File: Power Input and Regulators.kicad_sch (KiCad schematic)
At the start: 26 parts, among them J403 Screw_Terminal_01x03, U11 LD1117S33TR_SOT223, U12 LD1117S18TR_SOT223

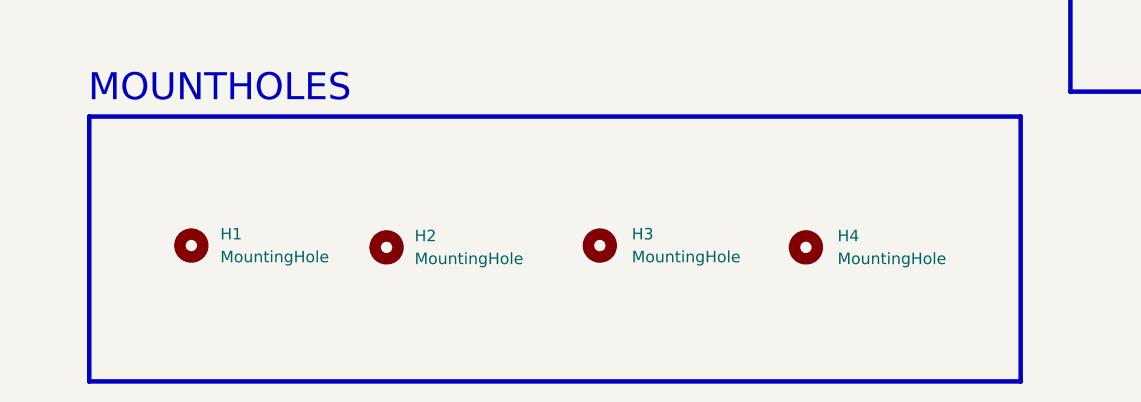
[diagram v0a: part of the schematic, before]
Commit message: All tracks routed, ERC done, waiting for PDN Analysis.
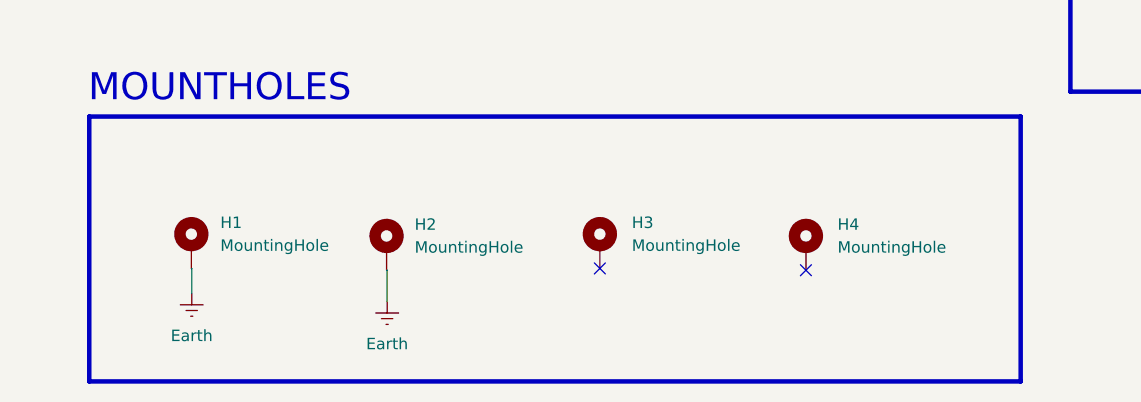
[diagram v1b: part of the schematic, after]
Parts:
- H1, H2, H3, H4: footprint MountingHole:MountingHole_2.1mm -> MountingHole:MountingHole_2.2mm_M2_DIN965_Pad; symbol Mechanical:MountingHole -> Mechanical:MountingHole_Pad; now left out of the parts list
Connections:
- new net Earth: H1.1, H2.1
- no-connect marks 0 -> 2
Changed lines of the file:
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@@
 		(color 0 0 0 0)
 	)
+	(no_connect
+		(at 122.221 152.7349)
+	)
+	(no_connect
+		(at 99.3247 152.5341)
+	)
 	(wire
 		(pts
@@
 	(wire
 		(pts
+			(xy 75.6884 156.2136) (xy 75.6884 152.7349)
+		)
+		(stroke
+			(width 0)
+			(type default)
+		)
+	)
+	(wire
+		(pts
 			(xy 183.6373 111.1069) (xy 183.6373 107.1757)
 		)
@@
 	(wire
 		(pts
+			(xy 53.9747 152.5341) (xy 53.934 152.5341)
+		)
+		(stroke
+			(width 0)
+			(type default)
+		)
+	)
+	(wire
+		(pts
 			(xy 58.4554 69.5105) (xy 58.4554 69.5604)
 		)
@@
 	(wire
 		(pts
+			(xy 75.6884 152.7349) (xy 75.6251 152.7349)
+		)
+		(stroke
+			(width 0)
+			(type default)
+		)
+	)
+	(wire
+		(pts
 			(xy 191.2089 122.2781) (xy 191.2089 122.441)
 		)
@@
 	(wire
 		(pts
+			(xy 53.9747 155.3066) (xy 53.9747 152.5341)
+		)
+		(stroke
+			(width 0)
+			(type default)
+		)
+	)
+	(wire
+		(pts
 			(xy 154.1008 47.327) (xy 154.1008 52.0459)
 		)
@@
 	)
 	(symbol
-		(lib_id "Mechanical:MountingHole")
+		(lib_id "Mechanical:MountingHole_Pad")
 		(at 99.3247 149.9941 0)
 		(unit 1)
-		(exclude_from_sim no)
-		(in_bom yes)
+		(exclude_from_sim yes)
+		(in_bom no)
 		(on_board yes)
 		(dnp no)
 		(fields_autoplaced yes)
 		(property "Reference" "H3"
-			(at 102.87 148.724 0)
+			(at 102.87 147.454 0)
 			(effects
 				(font
@@
 		)
 		(property "Value" "MountingHole"
-			(at 102.87 151.264 0)
+			(at 102.87 149.994 0)
 			(effects
 				(font
@@
 			)
 		)
-		(property "Footprint" "MountingHole:MountingHole_2.1mm"
+		(property "Footprint" "MountingHole:MountingHole_2.2mm_M2_DIN965_Pad"
 			(at 99.3247 149.9941 0)
 			(effects
@@
 			)
 		)
-		(property "Description" "Mounting Hole without connection"
+		(property "Description" "Mounting Hole with connection"
 			(at 99.3247 149.9941 0)
 			(effects
@@
 			)
 		)
+		(pin "1"
+		)
 		(instances
 			(project ""
@@
 	)
 	(symbol
+		(lib_id "power:Earth")
+		(at 53.9747 155.3066 0)
+		(unit 1)
+		(exclude_from_sim no)
+		(in_bom yes)
+		(on_board yes)
+		(dnp no)
+		(fields_autoplaced yes)
+		(property "Reference" "#PWR0416"
+			(at 53.9747 161.6566 0)
+			(effects
+				(font
+					(size 1.27 1.27)
+				)
+				(hide yes)
+			)
+		)
+		(property "Value" "Earth"
+			(at 53.9747 160.02 0)
+			(effects
+				(font
+					(size 1.27 1.27)
+				)
+			)
+		)
+		(property "Footprint" ""
+			(at 53.9747 155.3066 0)
+			(effects
+				(font
+					(size 1.27 1.27)
+				)
+				(hide yes)
+			)
+		)
+		(property "Datasheet" "~"
+			(at 53.9747 155.3066 0)
+			(effects
+				(font
+					(size 1.27 1.27)
+				)
+				(hide yes)
+			)
+		)
+		(property "Description" "Power symbol creates a global label with name \"Earth\""
+			(at 53.9747 155.3066 0)
+			(effects
+				(font
+					(size 1.27 1.27)
+				)
+				(hide yes)
+			)
+		)
+		(pin "1"
+		)
+		(instances
+			(project ""
+				(path "/8a424437-6f3e-424c-a786-3b8b285eee60/89ed5f6c-6a59-4754-9fdb-29c83f804302"
+					(reference "#PWR0416")
+					(unit 1)
+				)
+			)
+		)
+	)
+	(symbol
 		(lib_id "power:+12V")
 		(at 155.0312 102.4533 0)
@@
 	)
 	(symbol
+		(lib_id "power:Earth")
+		(at 75.6884 156.2136 0)
+		(unit 1)
+		(exclude_from_sim no)
+		(in_bom yes)
+		(on_board yes)
+		(dnp no)
+		(fields_autoplaced yes)
+		(property "Reference" "#PWR0102"
+			(at 75.6884 162.5636 0)
+			(effects
+				(font
+					(size 1.27 1.27)
+				)
+				(hide yes)
+			)
+		)
+		(property "Value" "Earth"
+			(at 75.6884 160.927 0)
+			(effects
+				(font
+					(size 1.27 1.27)
+				)
+			)
+		)
+		(property "Footprint" ""
+			(at 75.6884 156.2136 0)
+			(effects
+				(font
+					(size 1.27 1.27)
+				)
+				(hide yes)
+			)
+		)
+		(property "Datasheet" "~"
+			(at 75.6884 156.2136 0)
+			(effects
+				(font
+					(size 1.27 1.27)
+				)
+				(hide yes)
+			)
+		)
+		(property "Description" "Power symbol creates a global label with name \"Earth\""
+			(at 75.6884 156.2136 0)
+			(effects
+				(font
+					(size 1.27 1.27)
+				)
+				(hide yes)
+			)
+		)
+		(pin "1"
+		)
+		(instances
+			(project ""
+				(path "/8a424437-6f3e-424c-a786-3b8b285eee60/89ed5f6c-6a59-4754-9fdb-29c83f804302"
+					(reference "#PWR0102")
+					(unit 1)
+				)
+			)
+		)
+	)
+	(symbol
 		(lib_id "Connector:Screw_Terminal_01x03")
 		(at 48.2022 59.8852 0)
@@
 	)
 	(symbol
-		(lib_id "Mechanical:MountingHole")
+		(lib_id "Mechanical:MountingHole_Pad")
 		(at 53.934 149.9941 0)
 		(unit 1)
-		(exclude_from_sim no)
-		(in_bom yes)
+		(exclude_from_sim yes)
+		(in_bom no)
 		(on_board yes)
 		(dnp no)
 		(fields_autoplaced yes)
 		(property "Reference" "H1"
-			(at 57.15 148.724 0)
+			(at 57.15 147.454 0)
 			(effects
 				(font
@@
 		)
 		(property "Value" "MountingHole"
-			(at 57.15 151.264 0)
+			(at 57.15 149.994 0)
 			(effects
 				(font
@@
 			)
 		)
-		(property "Footprint" "MountingHole:MountingHole_2.1mm"
+		(property "Footprint" "MountingHole:MountingHole_2.2mm_M2_DIN965_Pad"
 			(at 53.934 149.9941 0)
 			(effects
@@
 			)
 		)
-		(property "Description" "Mounting Hole without connection"
+		(property "Description" "Mounting Hole with connection"
 			(at 53.934 149.9941 0)
 			(effects
@@
 			)
 		)
+		(pin "1"
+		)
 		(instances
 			(project ""
@@
 	)
 	(symbol
-		(lib_id "Mechanical:MountingHole")
+		(lib_id "Mechanical:MountingHole_Pad")
 		(at 122.221 150.1949 0)
 		(unit 1)
-		(exclude_from_sim no)
-		(in_bom yes)
+		(exclude_from_sim yes)
+		(in_bom no)
 		(on_board yes)
 		(dnp no)
 		(fields_autoplaced yes)
 		(property "Reference" "H4"
-			(at 125.73 148.9248 0)
+			(at 125.73 147.6548 0)
 			(effects
 				(font
@@
 		)
 		(property "Value" "MountingHole"
-			(at 125.73 151.4648 0)
+			(at 125.73 150.1948 0)
 			(effects
 				(font
@@
 			)
 		)
-		(property "Footprint" "MountingHole:MountingHole_2.1mm"
+		(property "Footprint" "MountingHole:MountingHole_2.2mm_M2_DIN965_Pad"
 			(at 122.221 150.1949 0)
 			(effects
@@
 			)
 		)
-		(property "Description" "Mounting Hole without connection"
+		(property "Description" "Mounting Hole with connection"
 			(at 122.221 150.1949 0)
 			(effects
@@
 			)
 		)
+		(pin "1"
+		)
 		(instances
 			(project ""
@@
 	)
 	(symbol
-		(lib_id "Mechanical:MountingHole")
+		(lib_id "Mechanical:MountingHole_Pad")
 		(at 75.6251 150.1949 0)
 		(unit 1)
-		(exclude_from_sim no)
-		(in_bom yes)
+		(exclude_from_sim yes)
+		(in_bom no)
 		(on_board yes)
 		(dnp no)
 		(fields_autoplaced yes)
 		(property "Reference" "H2"
-			(at 78.74 148.9248 0)
+			(at 78.74 147.6548 0)
 			(effects
 				(font
@@
 		)
 		(property "Value" "MountingHole"
-			(at 78.74 151.4648 0)
+			(at 78.74 150.1948 0)
 			(effects
 				(font
@@
 			)
 		)
-		(property "Footprint" "MountingHole:MountingHole_2.1mm"
+		(property "Footprint" "MountingHole:MountingHole_2.2mm_M2_DIN965_Pad"
 			(at 75.6251 150.1949 0)
 			(effects
@@
 			)
 		)
-		(property "Description" "Mounting Hole without connection"
+		(property "Description" "Mounting Hole with connection"
 			(at 75.6251 150.1949 0)
 			(effects
@@
 			)
 		)
+		(pin "1"
+		)
 		(instances

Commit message: schematic pages are reviewed
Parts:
- renumbered C14 to C11, C15 to C12, C11 to C13, C16 to C14, C12 to C15, C13 to C16, H1 to H11, H3 to H12, H2 to H13, H4 to H14, J403 to J11
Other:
- moved on the sheet: C13, C15, C16, H11, H12, H13, H14, J11
